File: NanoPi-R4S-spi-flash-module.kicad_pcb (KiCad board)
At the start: 4 copper layers, 30 x 13.2 mm, 22 parts, among them J1 NanoPi R4S, J2 TagConnect_TC2030_SWD, U1 W25Q32JVSS, U2 MX25R3235FZNxx0, U3 W25Q32JVSS, U4 MX25R3235FZNxx0, U5 STM32G031GxU

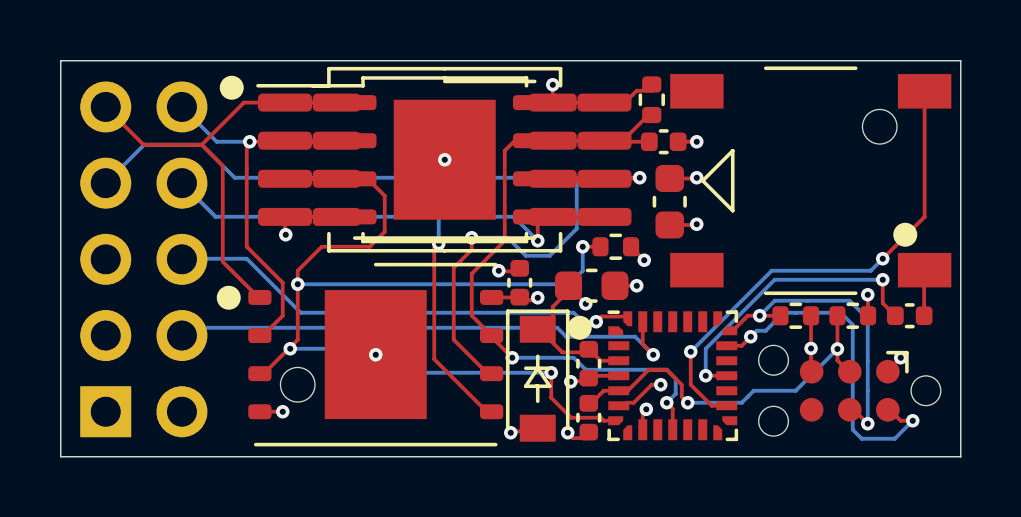
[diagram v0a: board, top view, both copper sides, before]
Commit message: Replace D1 by regular silicon diode
Schottky diodes tend to have high leakage current. Considering the MCU is
supposed to be kept running on C4 and C5 as long as possible after power
has been removed reducing leakage current back into the 3.3V supply rail
is key.
Replace D1 by an ordinary 1N4148 to minimize leakage current back into the
3.3V supply rail.
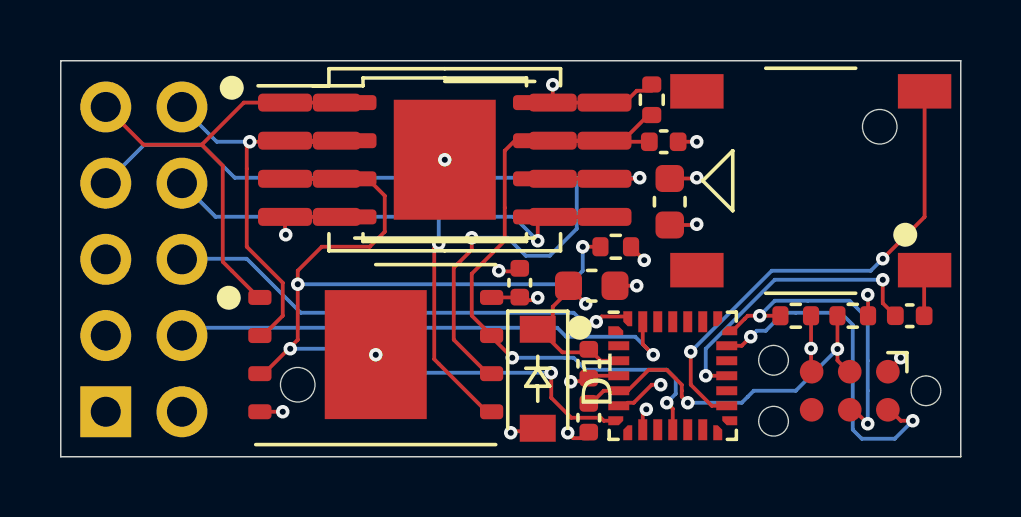
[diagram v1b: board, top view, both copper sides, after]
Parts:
- D1: value D_Schottky -> 1N4148W
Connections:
- C7 pad 1: GND -> /FLASH_~RST
- C7 pad 2: /FLASH_~RST -> GND
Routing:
- net GND: track 11.4 -> 10.7 mm, vias 11 -> 10
- net /FLASH_~RST: track 25.1 -> 25.7 mm, vias 2 -> 3
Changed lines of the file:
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@@
     (add_net "Net-(U5-Pad8)")
+  )
+  (module Diode_SMD:D_SOD-123 (layer F.Cu)
+    (at 46.2 37.2 270)
+    (descr SOD-123)
+    (tags SOD-123)
+    (attr smd)
+    (fp_text reference D1 (at 0 -2 90) (layer F.SilkS)
+      (effects (font (size 1 1) (thickness 0.15)))
+    )
+    (fp_text value 1N4148W (at 0 2.1 90) (layer F.Fab)
+      (effects (font (size 1 1) (thickness 0.15)))
+    )
+    (fp_text user %R (at 0 -2 90) (layer F.Fab)
+      (effects (font (size 1 1) (thickness 0.15)))
+    )
+    (fp_line (start -2.25 -1) (end -2.25 1) (layer F.SilkS) (width 0.12))
+    (fp_line (start 0.25 0) (end 0.75 0) (layer F.Fab) (width 0.1))
+    (fp_line (start 0.25 0.4) (end -0.35 0) (layer F.Fab) (width 0.1))
+    (fp_line (start 0.25 -0.4) (end 0.25 0.4) (layer F.Fab) (width 0.1))
+    (fp_line (start -0.35 0) (end 0.25 -0.4) (layer F.Fab) (width 0.1))
+    (fp_line (start -0.35 0) (end -0.35 0.55) (layer F.Fab) (width 0.1))
+    (fp_line (start -0.35 0) (end -0.35 -0.55) (layer F.Fab) (width 0.1))
+    (fp_line (start -0.75 0) (end -0.35 0) (layer F.Fab) (width 0.1))
+    (fp_line (start -1.4 0.9) (end -1.4 -0.9) (layer F.Fab) (width 0.1))
+    (fp_line (start 1.4 0.9) (end -1.4 0.9) (layer F.Fab) (width 0.1))
+    (fp_line (start 1.4 -0.9) (end 1.4 0.9) (layer F.Fab) (width 0.1))
+    (fp_line (start -1.4 -0.9) (end 1.4 -0.9) (layer F.Fab) (width 0.1))
+    (fp_line (start -2.35 -1.15) (end 2.35 -1.15) (layer F.CrtYd) (width 0.05))
+    (fp_line (start 2.35 -1.15) (end 2.35 1.15) (layer F.CrtYd) (width 0.05))
+    (fp_line (start 2.35 1.15) (end -2.35 1.15) (layer F.CrtYd) (width 0.05))
+    (fp_line (start -2.35 -1.15) (end -2.35 1.15) (layer F.CrtYd) (width 0.05))
+    (fp_line (start -2.25 1) (end 1.65 1) (layer F.SilkS) (width 0.12))
+    (fp_line (start -2.25 -1) (end 1.65 -1) (layer F.SilkS) (width 0.12))
+    (pad 2 smd rect (at 1.65 0 270) (size 0.9 1.2) (layers F.Cu F.Paste F.Mask)
+      (net 9 +3V3))
+    (pad 1 smd rect (at -1.65 0 270) (size 0.9 1.2) (layers F.Cu F.Paste F.Mask)
+      (net 30 "Net-(C3-Pad2)"))
+    (model ${KISYS3DMOD}/Diode_SMD.3dshapes/D_SOD-123.wrl
+      (at (xyz 0 0 0))
+      (scale (xyz 1 1 1))
+      (rotate (xyz 0 0 0))
+    )
   )
   (module Package_QFN_ST:Package_QFN_ST_ST_UFQFPN-28_4x4mm_P0.5mm (layer F.Cu)
@@
     (fp_line (start 0.91 0.46) (end -0.91 0.46) (layer F.CrtYd) (width 0.05))
     (pad 2 smd roundrect (at 0.48 0 180) (size 0.56 0.62) (layers F.Cu F.Paste F.Mask) (roundrect_rratio 0.25)
+      (net 6 GND))
+    (pad 1 smd roundrect (at -0.48 0 180) (size 0.56 0.62) (layers F.Cu F.Paste F.Mask) (roundrect_rratio 0.25)
       (net 15 /FLASH_~RST))
-    (pad 1 smd roundrect (at -0.48 0 180) (size 0.56 0.62) (layers F.Cu F.Paste F.Mask) (roundrect_rratio 0.25)
-      (net 6 GND))
     (model ${KISYS3DMOD}/Capacitor_SMD.3dshapes/C_0402_1005Metric.wrl
       (at (xyz 0 0 0))
@@
     (model ${KISYS3DMOD}/Buzzer_Beeper.3dshapes/MagneticBuzzer_Kobitone_254-EMB84Q-RO.wrl
       (at (xyz 0 0 0))
-      (scale (xyz 1 0.8 0.8))
-      (rotate (xyz 0 0 0))
-    )
-  )
-  (module Diode_SMD:D_SOD-123 (layer F.Cu)
-    (at 46.2 37.2 270)
-    (descr SOD-123)
-    (tags SOD-123)
-    (attr smd)
-    (fp_text reference D1 (at 0 -2 90) (layer F.SilkS) hide
-      (effects (font (size 1 1) (thickness 0.15)))
-    )
-    (fp_text value D_Schottky (at 0 2.1 90) (layer F.Fab)
-      (effects (font (size 1 1) (thickness 0.15)))
-    )
-    (fp_text user %R (at 0 -2 90) (layer F.Fab)
-      (effects (font (size 1 1) (thickness 0.15)))
-    )
-    (fp_line (start -2.25 -1) (end -2.25 1) (layer F.SilkS) (width 0.12))
-    (fp_line (start 0.25 0) (end 0.75 0) (layer F.Fab) (width 0.1))
-    (fp_line (start 0.25 0.4) (end -0.35 0) (layer F.Fab) (width 0.1))
-    (fp_line (start 0.25 -0.4) (end 0.25 0.4) (layer F.Fab) (width 0.1))
-    (fp_line (start -0.35 0) (end 0.25 -0.4) (layer F.Fab) (width 0.1))
-    (fp_line (start -0.35 0) (end -0.35 0.55) (layer F.Fab) (width 0.1))
-    (fp_line (start -0.35 0) (end -0.35 -0.55) (layer F.Fab) (width 0.1))
-    (fp_line (start -0.75 0) (end -0.35 0) (layer F.Fab) (width 0.1))
-    (fp_line (start -1.4 0.9) (end -1.4 -0.9) (layer F.Fab) (width 0.1))
-    (fp_line (start 1.4 0.9) (end -1.4 0.9) (layer F.Fab) (width 0.1))
-    (fp_line (start 1.4 -0.9) (end 1.4 0.9) (layer F.Fab) (width 0.1))
-    (fp_line (start -1.4 -0.9) (end 1.4 -0.9) (layer F.Fab) (width 0.1))
-    (fp_line (start -2.35 -1.15) (end 2.35 -1.15) (layer F.CrtYd) (width 0.05))
-    (fp_line (start 2.35 -1.15) (end 2.35 1.15) (layer F.CrtYd) (width 0.05))
-    (fp_line (start 2.35 1.15) (end -2.35 1.15) (layer F.CrtYd) (width 0.05))
-    (fp_line (start -2.35 -1.15) (end -2.35 1.15) (layer F.CrtYd) (width 0.05))
-    (fp_line (start -2.25 1) (end 1.65 1) (layer F.SilkS) (width 0.12))
-    (fp_line (start -2.25 -1) (end 1.65 -1) (layer F.SilkS) (width 0.12))
-    (pad 2 smd rect (at 1.65 0 270) (size 0.9 1.2) (layers F.Cu F.Paste F.Mask)
-      (net 9 +3V3))
-    (pad 1 smd rect (at -1.65 0 270) (size 0.9 1.2) (layers F.Cu F.Paste F.Mask)
-      (net 30 "Net-(C3-Pad2)"))
-    (model ${KISYS3DMOD}/Diode_SMD.3dshapes/D_SOD-123.wrl
-      (at (xyz 0 0 0))
-      (scale (xyz 1 1 1))
+      (scale (xyz 0.9 0.8 0.8))
       (rotate (xyz 0 0 0))
     )
@@
     (model ${KISYS3DMOD}/Package_SON.3dshapes/WSON-8_4x4mm_P0.8mm.wrl
       (at (xyz 0 0 0))
-      (scale (xyz 1.9 1.5 1.5))
+      (scale (xyz 1.8 1.5 1.5))
       (rotate (xyz 0 0 0))
     )
@@
   (via (at 49.5 34.1) (size 0.45) (drill 0.2) (layers F.Cu B.Cu) (net 6))
   (segment (start 48.775 34.1) (end 49.5 34.1) (width 0.127) (layer F.Cu) (net 6))
-  (via (at 51.5 29.3) (size 0.45) (drill 0.2) (layers F.Cu B.Cu) (net 6))
-  (segment (start 50.88 29.3) (end 51.5 29.3) (width 0.127) (layer F.Cu) (net 6))
+  (via (at 51.5 29.3) (size 0.45) (drill 0.2) (layers F.Cu B.Cu) (net 15))
+  (segment (start 50.88 29.3) (end 51.5 29.3) (width 0.127) (layer F.Cu) (net 15))
   (via (at 47.2 39) (size 0.45) (drill 0.2) (layers F.Cu B.Cu) (net 6))
   (segment (start 47.38 39.18) (end 47.2 39) (width 0.127) (layer F.Cu) (net 6))
